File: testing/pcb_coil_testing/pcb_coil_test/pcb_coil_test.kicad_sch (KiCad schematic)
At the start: 18 parts

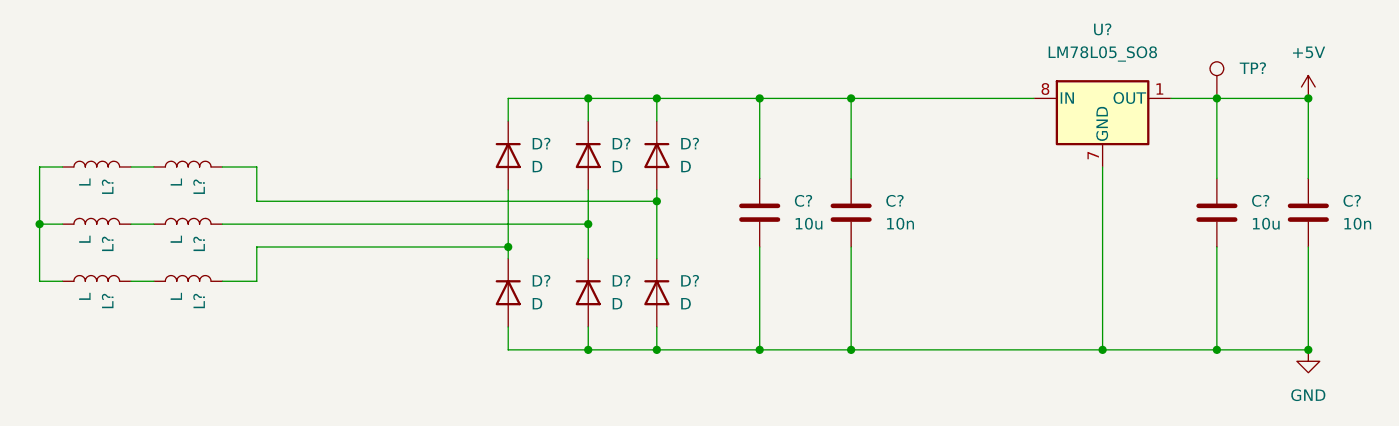
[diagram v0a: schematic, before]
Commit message: ordered pcb coil testing boards
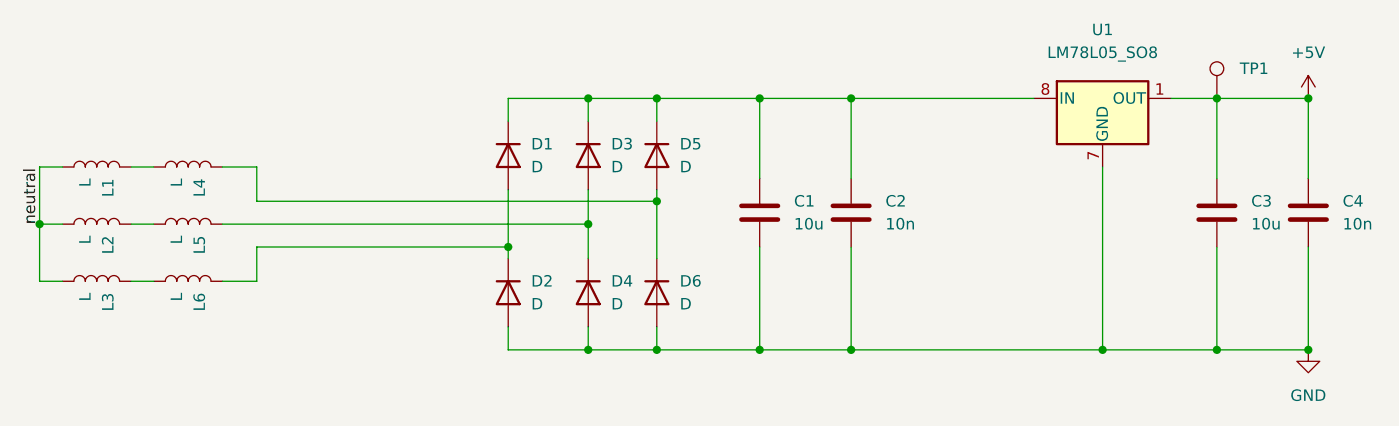
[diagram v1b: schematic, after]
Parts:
- C1, C3: renamed from C?; footprint (none) -> Capacitor_THT:CP_Radial_D5.0mm_P2.50mm
- C2, C4: renamed from C?; footprint (none) -> Capacitor_THT:C_Rect_L7.0mm_W2.0mm_P5.00mm
- D1, D2, D3, D4, D5, D6: renamed from D?; footprint (none) -> Diode_THT:D_A-405_P10.16mm_Horizontal
- L1, L2, L3, L4, L5, L6: renamed from L?; footprint (none) -> Library:pcb_coil
- TP1: renamed from TP?; footprint (none) -> TestPoint:TestPoint_Keystone_5010-5014_Multipurpose
- gave numbers to parts that had none: 1
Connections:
- net neutral: now reaches L1.1, L2.1, L3.1
